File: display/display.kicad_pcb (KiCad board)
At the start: 2 copper layers, 32.5 x 13.5 mm, 14 parts, among them P1 51281-1094, P2 CONN_9

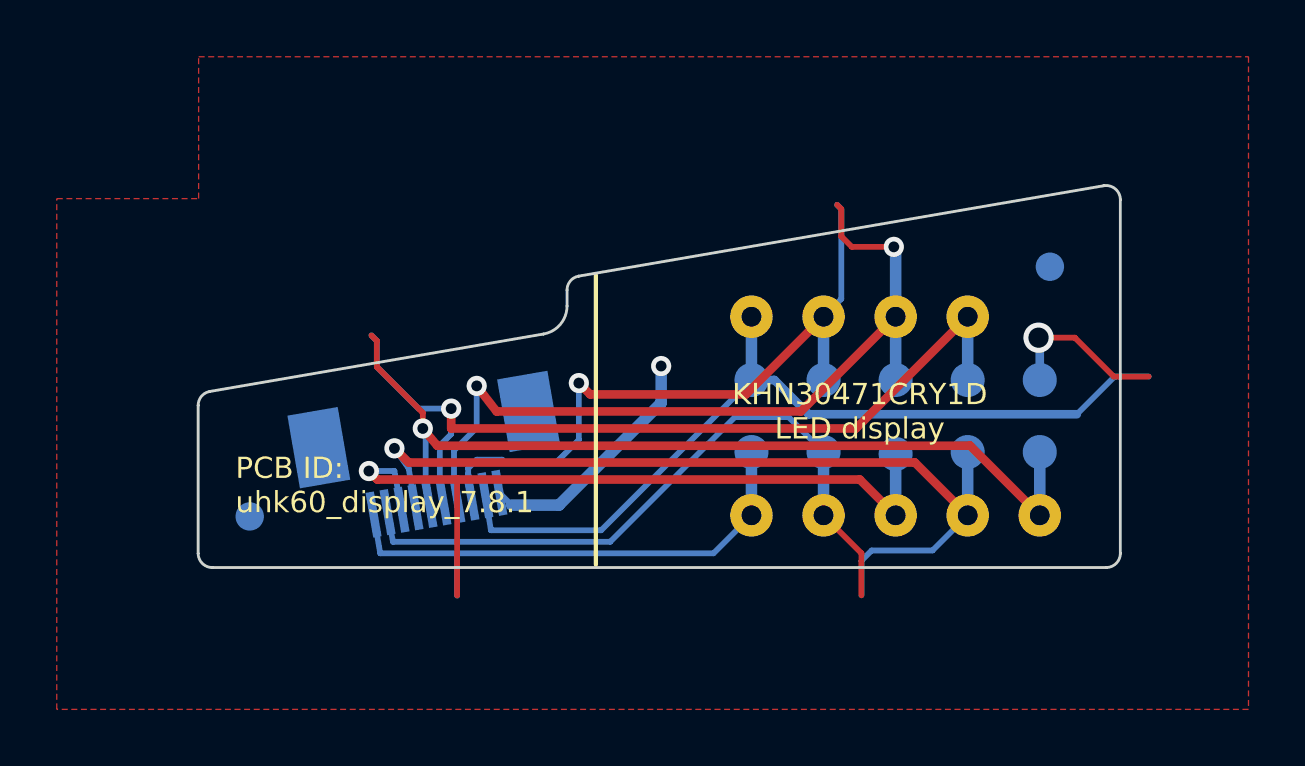
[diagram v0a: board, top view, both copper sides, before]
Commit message: New display board (update schematic and pcb).
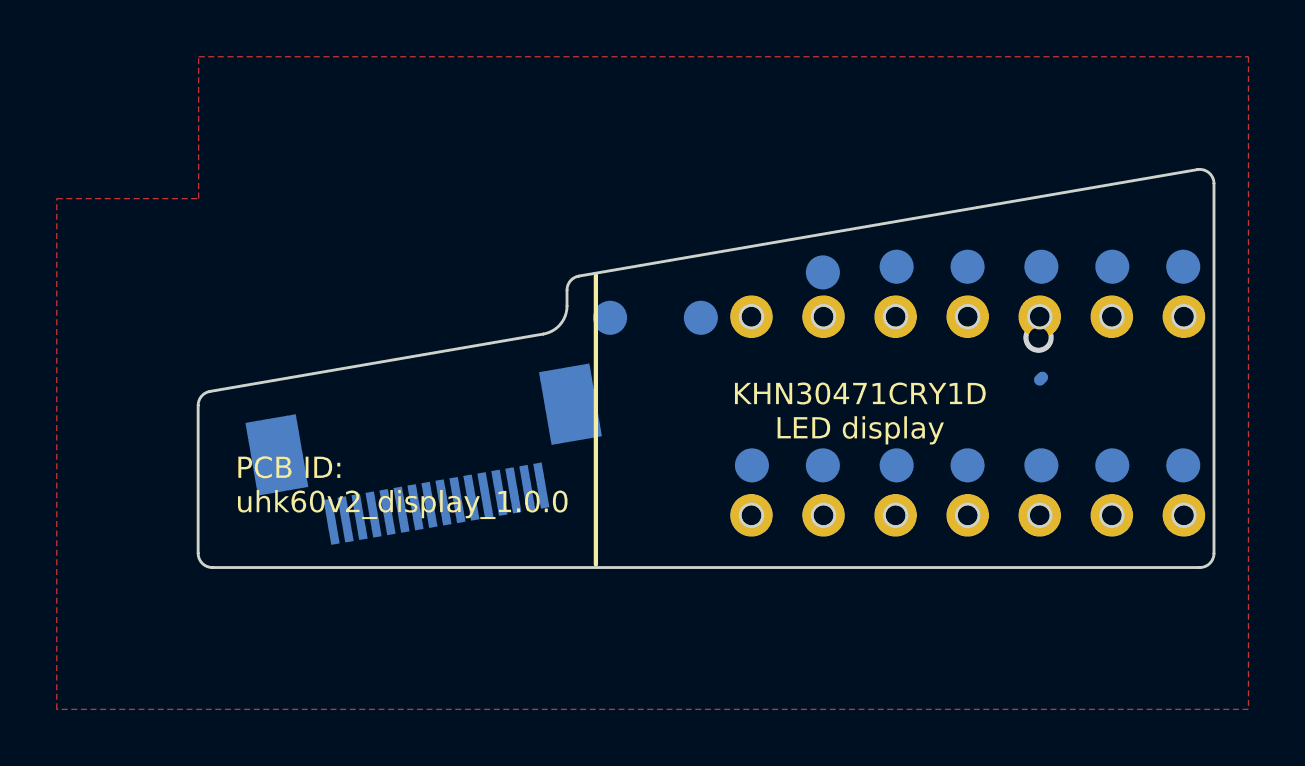
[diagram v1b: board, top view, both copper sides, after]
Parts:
- removed FID1, FID2: FIDUCIAL, Input_Club:FID
- removed TP_CB1: CB1, UGL:Test_Point
- removed TP_CB2: CB2, UGL:Test_Point
- removed TP_CB3: CB3, UGL:Test_Point
- removed TP_CB4: CB4, UGL:Test_Point
- removed TP_CB5: CB5, UGL:Test_Point
- removed TP_CB6: CB6, UGL:Test_Point
- removed TP_CB7: CB7, UGL:Test_Point
- removed TP_CB8: CB8, UGL:Test_Point
- removed TP_CB9: CB9, UGL:Test_Point
- added TP_CS1: CS1, UGL:Test_Point, B.Cu at (156.6, 105.5)
- added TP_CS2: CS2, UGL:Test_Point, B.Cu at (156.6, 98.5)
- added TP_CS3: CS3, UGL:Test_Point, B.Cu at (154.1, 98.5)
- added TP_CS4: CS4, UGL:Test_Point, B.Cu at (151.6, 98.5)
- added TP_CS5: CS5, UGL:Test_Point, B.Cu at (149.0, 98.5)
- added TP_CS6: CS6, UGL:Test_Point, B.Cu at (146.5, 98.5)
- added TP_CS7: CS7, UGL:Test_Point, B.Cu at (143.9, 98.7)
- added TP_CS8: CS8, UGL:Test_Point, B.Cu at (139.6, 100.3)
- added TP_SW10: SW10, UGL:Test_Point, B.Cu at (149.0, 105.5)
- added TP_SW11: SW11, UGL:Test_Point, B.Cu at (151.6, 105.5)
- added TP_SW12: SW12, UGL:Test_Point, B.Cu at (154.1, 105.5)
- added TP_SW7: SW7, UGL:Test_Point, B.Cu at (141.4, 105.5)
- added TP_SW8: SW8, UGL:Test_Point, B.Cu at (143.9, 105.5)
- added TP_SW9: SW9, UGL:Test_Point, B.Cu at (146.5, 105.5)
- P1: value 51281-1094 -> 51281-1694; footprint UGL:FFC_Connector_51281-1094 -> UGL:FFC_Connector_51281-1694
- P2: value CONN_9 -> CONN_14; footprint UGL:UHK_LED_display -> UGL:UHK_LED_display_multiplexed
- moved TP_GND1 15.3 mm to (136.4, 100.3)
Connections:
- net /CB1 renamed /SW7
- net /CB2 renamed /SW8
- net /CB3 renamed /SW9
- net /CB4 renamed /SW10
- net /CB5 renamed /SW11
- net /CB6 renamed /SW12
- P1 pad 10: GND -> /CS3
- P1 pad 7: /CB7 -> Net-(P1-Pad7)
- P1 pad 8: /CB8 -> /CS1
- P1 pad 9: /CB9 -> /CS2
- P2 pad 7: /CB7 -> /CS1
- P2 pad 8: /CB8 -> /CS2
- P2 pad 9: /CB9 -> /CS3
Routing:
- net /SW11: track 32.1 -> 0.00 mm, vias 1 -> 0
- net /SW10: track 31.3 -> 0.00 mm, vias 1 -> 0
- net /SW12: track 30.7 -> 0.00 mm, vias 1 -> 0
- net /CB9: track 30.0 -> 0.00 mm
- net /CB7: track 28.9 -> 0.00 mm, vias 2 -> 0
- net /SW9: track 27.7 -> 0.00 mm, vias 1 -> 0
- net /SW8: track 24.2 -> 0.00 mm
- net /CB8: track 23.9 -> 0.00 mm, vias 1 -> 0
- net /SW7: track 18.7 -> 0.00 mm
- net GND: track 14.8 -> 0.13 mm, vias 2 -> 0
- net /CS4: track 0.00 -> 0.06 mm, vias 0 -> 1
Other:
- board size 32.5 x 13.5 mm -> 35.8 x 14 mm
- board text added: "PCB ID: uhk60v2_display_1.0.0"
- board text removed: "PCB ID: uhk60_display_7.8.1"

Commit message: Wired display board.
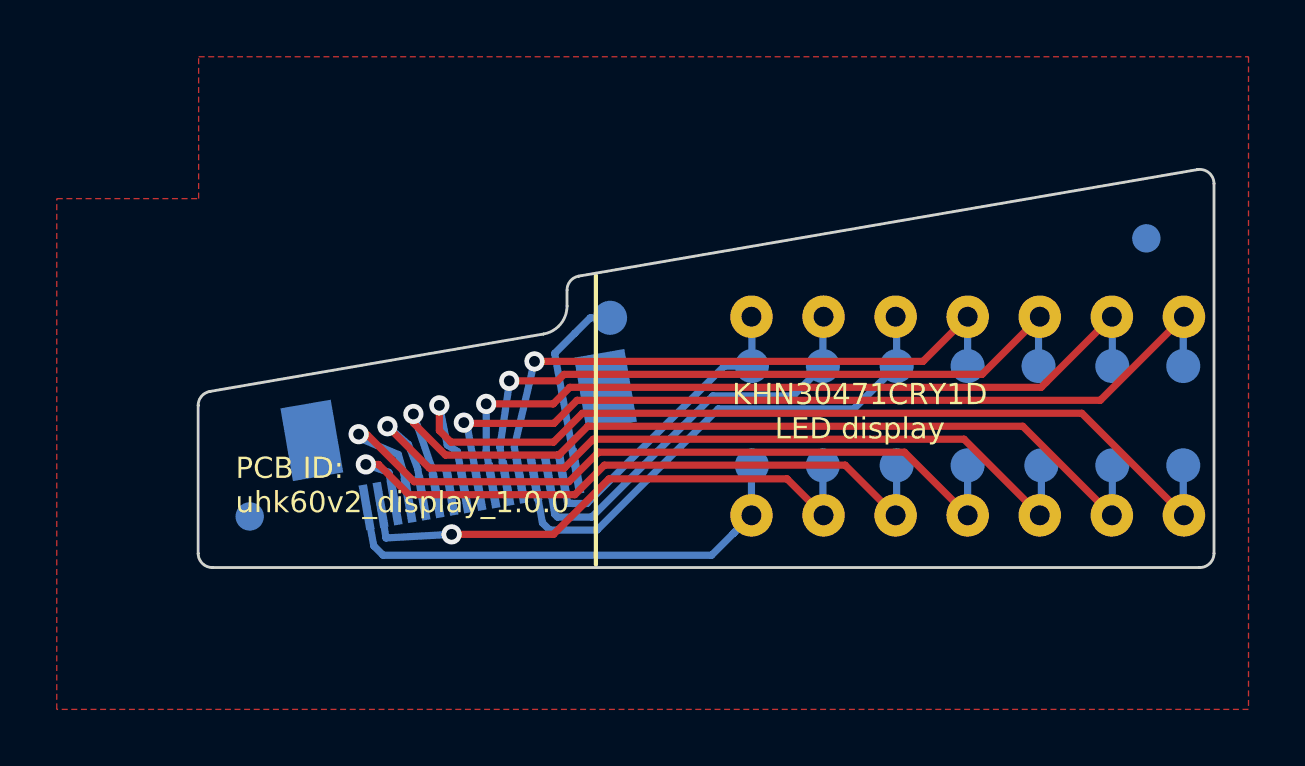
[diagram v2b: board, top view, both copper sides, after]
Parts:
- added FID1: >VALUE, Input_Club:FID, B.Cu at (123.7, 107.3)
- added FID2: >VALUE, Input_Club:FID, B.Cu at (155.3, 97.5)
- moved TP_CS4 3.50 mm to (151.5, 102.0)
- moved TP_CS2 3.50 mm to (156.6, 102.0)
- moved TP_CS3 3.50 mm to (154.1, 102.0)
- moved TP_CS5 3.50 mm to (149.0, 102.0)
- moved TP_CS6 3.50 mm to (146.5, 102.0)
- moved TP_CS7 3.30 mm to (143.9, 102.0)
- moved TP_CS8 2.48 mm to (141.4, 102.0)
- moved P1 1.33 mm to (130.8, 102.2)
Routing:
- net /CS1: track 0.00 -> 34.2 mm, vias 0 -> 1
- net /SW12: track 0.00 -> 31.9 mm, vias 0 -> 1
- net /CS2: track 0.00 -> 30.8 mm, vias 0 -> 1
- net /SW11: track 0.00 -> 29.9 mm, vias 0 -> 1
- net /SW10: track 0.00 -> 28.3 mm, vias 0 -> 1
- net /CS3: track 0.00 -> 28.0 mm, vias 0 -> 1
- net /CS4: track 0.06 -> 24.9 mm
- net /SW9: track 0.00 -> 24.0 mm, vias 0 -> 1
- net /CS5: track 0.00 -> 22.0 mm, vias 0 -> 1
- net /SW8: track 0.00 -> 19.7 mm, vias 0 -> 1
- net /CS6: track 0.00 -> 18.3 mm
- net /SW7: track 0.00 -> 17.3 mm
- net /CS7: track 0.00 -> 14.8 mm
- net /CS8: track 0.00 -> 11.3 mm
- net GND: track 0.13 -> 6.69 mm
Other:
- outline, holes or cut-outs redrawn

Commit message: Add GND plane on display pcb.
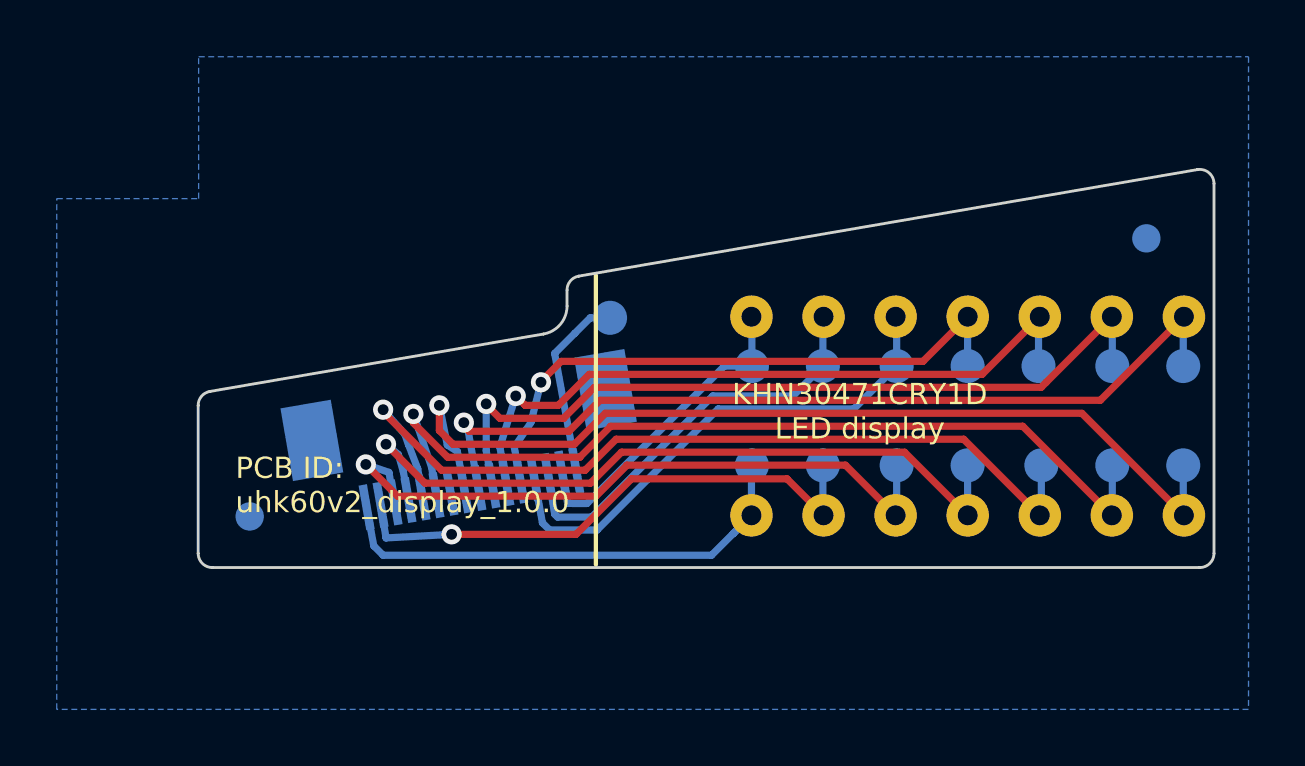
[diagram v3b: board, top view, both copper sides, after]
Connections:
- P1 pad : (no net) -> GND
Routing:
- net /SW10: track 28.3 -> 26.4 mm
- net /SW11: track 29.9 -> 30.8 mm
- net /CS5: track 22.0 -> 21.4 mm
- added copper zone on B.Cu, net GND
- removed copper zone on F.Cu, net GND

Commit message: DRC error fixed on display board.
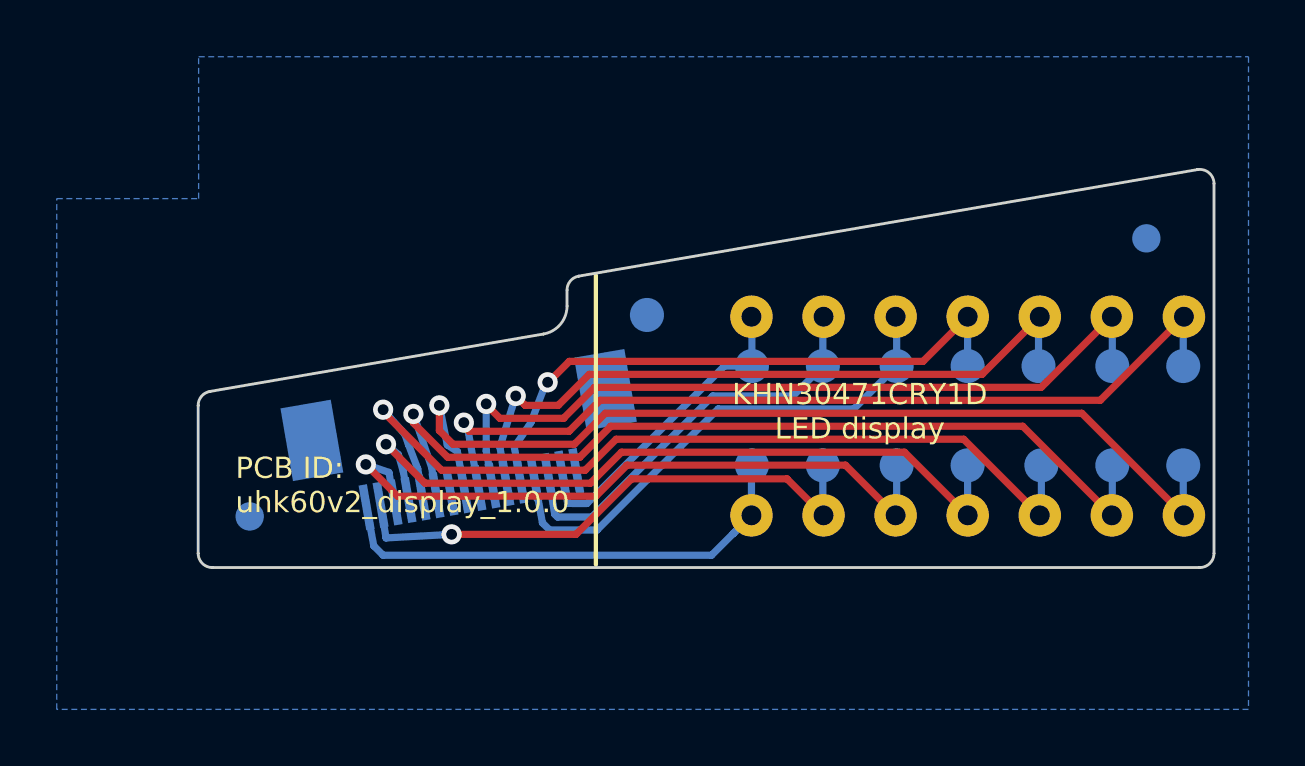
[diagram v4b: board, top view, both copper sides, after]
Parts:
- moved TP_GND1 1.30 mm to (137.7, 100.2)
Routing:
- net GND: track 6.69 -> 0.00 mm
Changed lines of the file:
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@@
     (thickness 1.6002)
     (drawings 47)
-    (tracks 145)
+    (tracks 141)
     (zones 0)
     (modules 19)
@@
   )
   (setup
-    (last_trace_width 0.254)
+    (last_trace_width 0.3048)
     (user_trace_width 0.2032)
     (user_trace_width 0.254)
@@
     (pad 15 smd rect (at 3.25 4.2 9.8) (size 0.3 1.6) (layers B.Cu B.Paste B.Mask)
       (net 10 /CS8) (clearance 0.1778))
-    (pad 16 smd rect (at 3.75 4.200001 9.8) (size 0.3 1.6) (layers B.Cu B.Paste B.Mask)
+    (pad 16 smd rect (at 3.75 4.200002 9.8) (size 0.3 1.6) (layers B.Cu B.Paste B.Mask)
       (net 1 GND) (clearance 0.1778))
   )
   (module UGL:Test_Point (layer B.Cu)
-    (at 136.375 100.275 180)
+    (at 137.675 100.175 180)
     (descr FID)
     (tags FIDUCIAL)
@@
       (effects (font (size 0.75 0.75) (thickness 0.15)) (justify mirror))
     )
-    (fp_text value GND (at -1.6 -0.1 270) (layer B.SilkS)
+    (fp_text value GND (at 0 -1.3) (layer B.SilkS)
       (effects (font (size 0.75 0.75) (thickness 0.15)) (justify mirror))
     )
@@
       (effects (font (size 0.75 0.75) (thickness 0.15)) (justify mirror))
     )
-    (fp_text value CS2 (at 0 -1.3) (layer B.SilkS)
+    (fp_text value CS2 (at 0 1.2) (layer B.SilkS)
       (effects (font (size 0.75 0.75) (thickness 0.15)) (justify mirror))
     )
@@
       (effects (font (size 0.75 0.75) (thickness 0.15)) (justify mirror))
     )
-    (fp_text value CS3 (at 0 -1.3) (layer B.SilkS)
+    (fp_text value CS3 (at 0 1.2) (layer B.SilkS)
       (effects (font (size 0.75 0.75) (thickness 0.15)) (justify mirror))
     )
@@
       (effects (font (size 0.75 0.75) (thickness 0.15)) (justify mirror))
     )
-    (fp_text value CS4 (at 0 -1.3) (layer B.SilkS)
+    (fp_text value CS4 (at 0 1.2) (layer B.SilkS)
       (effects (font (size 0.75 0.75) (thickness 0.15)) (justify mirror))
     )
@@
       (effects (font (size 0.75 0.75) (thickness 0.15)) (justify mirror))
     )
-    (fp_text value CS5 (at 0 -1.3) (layer B.SilkS)
+    (fp_text value CS5 (at 0 1.2) (layer B.SilkS)
       (effects (font (size 0.75 0.75) (thickness 0.15)) (justify mirror))
     )
@@
       (effects (font (size 0.75 0.75) (thickness 0.15)) (justify mirror))
     )
-    (fp_text value CS6 (at 0 -1.3) (layer B.SilkS)
+    (fp_text value CS6 (at 0 1.2) (layer B.SilkS)
       (effects (font (size 0.75 0.75) (thickness 0.15)) (justify mirror))
     )
@@
       (effects (font (size 0.75 0.75) (thickness 0.15)) (justify mirror))
     )
-    (fp_text value CS7 (at 0 -1.3) (layer B.SilkS)
+    (fp_text value CS7 (at 0 1.2) (layer B.SilkS)
       (effects (font (size 0.75 0.75) (thickness 0.15)) (justify mirror))
     )
@@
       (effects (font (size 0.75 0.75) (thickness 0.15)) (justify mirror))
     )
-    (fp_text value CS8 (at 0 -1.3) (layer B.SilkS)
+    (fp_text value CS8 (at 0.1 1.2) (layer B.SilkS)
       (effects (font (size 0.75 0.75) (thickness 0.15)) (justify mirror))
     )
@@
     (effects (font (size 1.5 1.5) (thickness 0.3)) (justify left mirror))
   )
-  (segment (start 135.18516 105.675428) (end 134.4226 101.5312) (width 0.254) (layer B.Cu) (net 1))
-  (segment (start 135.6788 100.275) (end 136.375 100.275) (width 0.254) (layer B.Cu) (net 1))
-  (segment (start 134.4226 101.5312) (end 135.1338 100.82) (width 0.254) (layer B.Cu) (net 1))
-  (segment (start 135.1338 100.82) (end 135.6788 100.275) (width 0.254) (layer B.Cu) (net 1))
   (segment (start 127.7946 106.951999) (end 128.0472 108.313) (width 0.254) (layer B.Cu) (net 2))
   (segment (start 128.3774 108.6432) (end 139.951491 108.6432) (width 0.254) (layer B.Cu) (net 2))
@@
   (segment (start 148.975 101.975) (end 148.975 100.239691) (width 0.254) (layer B.Cu) (net 7))
   (segment (start 133.214344 106.015847) (end 133.0002 104.8332) (width 0.254) (layer B.Cu) (net 7))
-  (via (at 133.94 102.5472) (size 0.7112) (drill 0.381) (layers F.Cu B.Cu) (net 7))
+  (via (at 134.175 102.5472) (size 0.7112) (drill 0.381) (layers F.Cu B.Cu) (net 7))
+  (segment (start 133.0002 104.8332) (end 133.5844 103.9696) (width 0.254) (layer B.Cu) (net 7))
   (segment (start 147.404091 101.8106) (end 148.978261 100.23643) (width 0.254) (layer F.Cu) (net 7))
-  (segment (start 133.94 102.5218) (end 134.6512 101.8106) (width 0.254) (layer F.Cu) (net 7))
-  (segment (start 134.6512 101.8106) (end 147.404091 101.8106) (width 0.254) (layer F.Cu) (net 7))
-  (segment (start 133.0002 104.8332) (end 133.5844 103.9696) (width 0.254) (layer B.Cu) (net 7))
-  (segment (start 133.5844 103.9696) (end 133.94 102.5472) (width 0.254) (layer B.Cu) (net 7))
+  (segment (start 134.175 102.575) (end 134.9394 101.8106) (width 0.254) (layer F.Cu) (net 7))
+  (segment (start 134.9394 101.8106) (end 147.404091 101.8106) (width 0.254) (layer F.Cu) (net 7))
+  (segment (start 133.5844 103.9696) (end 134.120678 102.557196) (width 0.254) (layer B.Cu) (net 7))
   (segment (start 146.475 100.273169) (end 146.438261 100.23643) (width 0.254) (layer B.Cu) (net 8))
   (segment (start 146.475 101.975) (end 146.475 100.273169) (width 0.254) (layer B.Cu) (net 8))

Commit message: Display FFC pinout changed.
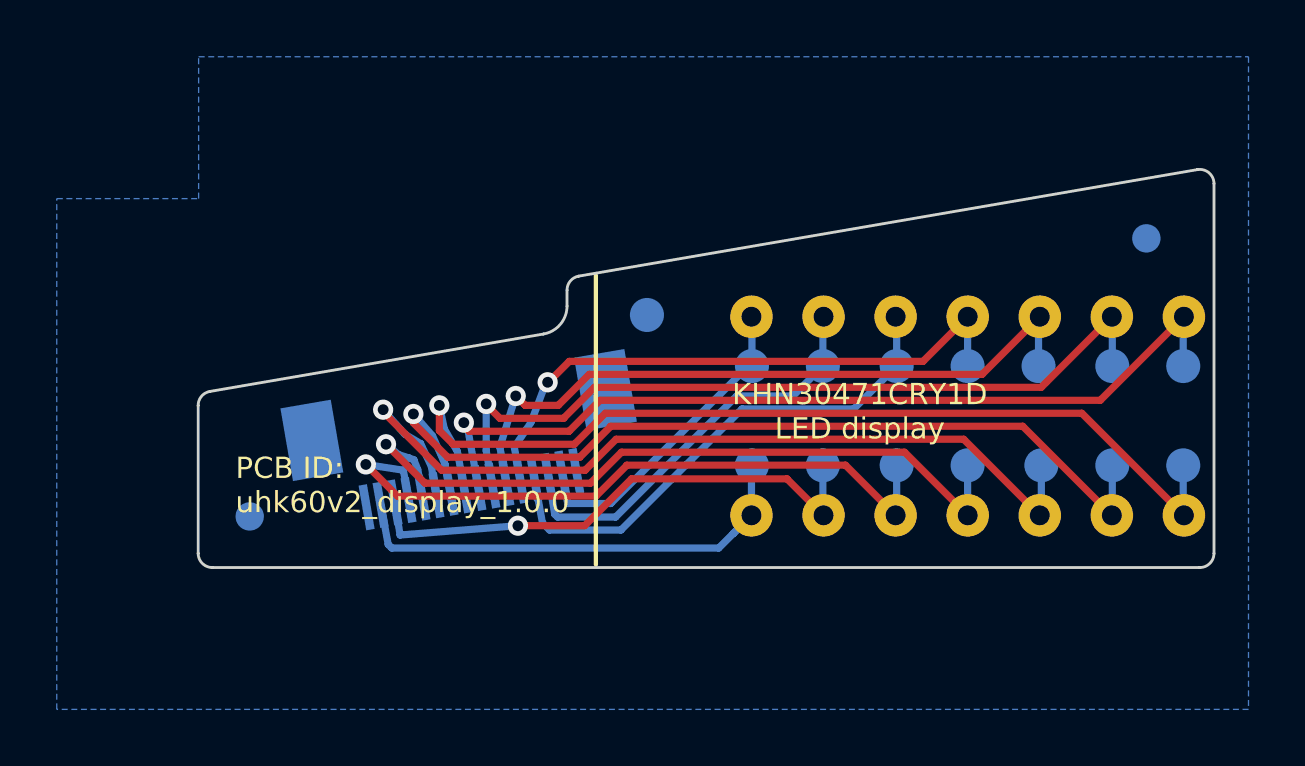
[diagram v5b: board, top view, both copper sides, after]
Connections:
- P1 pad 1: /SW7 -> GND
- P1 pad 2: /SW8 -> /SW7
- P1 pad 3: /SW9 -> /SW8
- P1 pad 4: /SW10 -> /SW9
- P1 pad 5: /SW11 -> /SW10
- P1 pad 6: /SW12 -> /SW11
- P1 pad 7: Net-(P1-Pad7) -> /SW12
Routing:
- net /SW7: track 17.3 -> 16.6 mm
- net /SW8: track 19.7 -> 19.1 mm
